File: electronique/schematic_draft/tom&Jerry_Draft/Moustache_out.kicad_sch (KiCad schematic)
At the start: 4 parts, among them J2001 Conn_01x02

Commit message: Adding footprint V0.1
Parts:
- C2001: footprint (none) -> Capacitor_SMD:C_0402_1005Metric
- J2001: footprint (none) -> Connector_JST:JST_XH_S2B-XH-A-1_1x02_P2.50mm_Horizontal
- R2001, R2002: footprint (none) -> Resistor_SMD:R_0402_1005Metric
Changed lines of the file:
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@@
 			)
 		)
-		(property "Footprint" ""
+		(property "Footprint" "Resistor_SMD:R_0402_1005Metric"
 			(at 143.51 72.39 0)
 			(effects
@@
 			)
 		)
-		(property "Footprint" ""
+		(property "Footprint" "Connector_JST:JST_XH_S2B-XH-A-1_1x02_P2.50mm_Horizontal"
 			(at 156.21 77.47 0)
 			(effects
@@
 			)
 		)
-		(property "Footprint" ""
+		(property "Footprint" "Resistor_SMD:R_0402_1005Metric"
 			(at 151.13 67.31 0)
 			(effects
@@
 			)
 		)
-		(property "Footprint" ""
+		(property "Footprint" "Capacitor_SMD:C_0402_1005Metric"
 			(at 137.16 77.47 0)
 			(effects

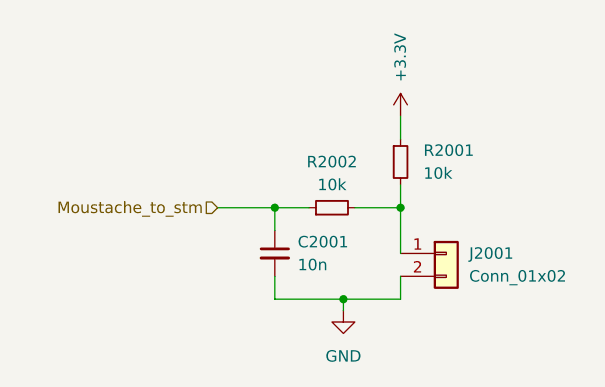
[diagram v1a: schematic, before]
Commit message: Ajout V2 TOF + MultiPCB Panalize
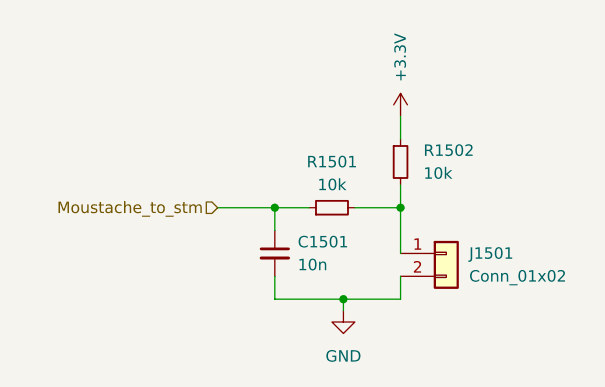
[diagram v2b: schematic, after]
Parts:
- renumbered C2001 to C1501, J2001 to J1501, R2002 to R1501, R2001 to R1502
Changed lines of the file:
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@@
 		(dnp no)
 		(fields_autoplaced yes)
-		(property "Reference" "R2002"
+		(property "Reference" "R1501"
 			(at 143.51 67.31 90)
 			(effects
@@
 			(project "tom&Jerry_Draft"
 				(path "/d6e3fbeb-d028-494d-83bf-2e4a8b12578d/ac7f7f04-c418-4551-b204-a999b9c3c440/4a942aeb-0f5a-4b74-98aa-4f22cccd5125"
-					(reference "R2002")
-					(unit 1)
-				)
-				(path "/d6e3fbeb-d028-494d-83bf-2e4a8b12578d/ac7f7f04-c418-4551-b204-a999b9c3c440/a23499ad-e269-4d60-8a7e-fdf0e52e9311"
-					(reference "R1702")
-					(unit 1)
-				)
-				(path "/d6e3fbeb-d028-494d-83bf-2e4a8b12578d/ac7f7f04-c418-4551-b204-a999b9c3c440/e8ed5780-2114-4427-a772-5bf6fa774e5b"
-					(reference "R1902")
-					(unit 1)
-				)
-				(path "/d6e3fbeb-d028-494d-83bf-2e4a8b12578d/ac7f7f04-c418-4551-b204-a999b9c3c440/e9c92678-eab0-4500-8304-4b18da6b06b1"
-					(reference "R1802")
+					(reference "R1501")
+					(unit 1)
+				)
+				(path "/d6e3fbeb-d028-494d-83bf-2e4a8b12578d/ac7f7f04-c418-4551-b204-a999b9c3c440/a23499ad-e269-4d60-8a7e-fdf0e52e9311"
+					(reference "R1201")
+					(unit 1)
+				)
+				(path "/d6e3fbeb-d028-494d-83bf-2e4a8b12578d/ac7f7f04-c418-4551-b204-a999b9c3c440/e8ed5780-2114-4427-a772-5bf6fa774e5b"
+					(reference "R1401")
+					(unit 1)
+				)
+				(path "/d6e3fbeb-d028-494d-83bf-2e4a8b12578d/ac7f7f04-c418-4551-b204-a999b9c3c440/e9c92678-eab0-4500-8304-4b18da6b06b1"
+					(reference "R1301")
 					(unit 1)
 				)
@@
 		(dnp no)
 		(fields_autoplaced yes)
-		(property "Reference" "J2001"
+		(property "Reference" "J1501"
 			(at 158.75 77.4699 0)
 			(effects
@@
 			(project "tom&Jerry_Draft"
 				(path "/d6e3fbeb-d028-494d-83bf-2e4a8b12578d/ac7f7f04-c418-4551-b204-a999b9c3c440/4a942aeb-0f5a-4b74-98aa-4f22cccd5125"
-					(reference "J2001")
-					(unit 1)
-				)
-				(path "/d6e3fbeb-d028-494d-83bf-2e4a8b12578d/ac7f7f04-c418-4551-b204-a999b9c3c440/a23499ad-e269-4d60-8a7e-fdf0e52e9311"
-					(reference "J1701")
-					(unit 1)
-				)
-				(path "/d6e3fbeb-d028-494d-83bf-2e4a8b12578d/ac7f7f04-c418-4551-b204-a999b9c3c440/e8ed5780-2114-4427-a772-5bf6fa774e5b"
-					(reference "J1901")
-					(unit 1)
-				)
-				(path "/d6e3fbeb-d028-494d-83bf-2e4a8b12578d/ac7f7f04-c418-4551-b204-a999b9c3c440/e9c92678-eab0-4500-8304-4b18da6b06b1"
-					(reference "J1801")
+					(reference "J1501")
+					(unit 1)
+				)
+				(path "/d6e3fbeb-d028-494d-83bf-2e4a8b12578d/ac7f7f04-c418-4551-b204-a999b9c3c440/a23499ad-e269-4d60-8a7e-fdf0e52e9311"
+					(reference "J1201")
+					(unit 1)
+				)
+				(path "/d6e3fbeb-d028-494d-83bf-2e4a8b12578d/ac7f7f04-c418-4551-b204-a999b9c3c440/e8ed5780-2114-4427-a772-5bf6fa774e5b"
+					(reference "J1401")
+					(unit 1)
+				)
+				(path "/d6e3fbeb-d028-494d-83bf-2e4a8b12578d/ac7f7f04-c418-4551-b204-a999b9c3c440/e9c92678-eab0-4500-8304-4b18da6b06b1"
+					(reference "J1301")
 					(unit 1)
 				)
@@
 		(dnp no)
 		(fields_autoplaced yes)
-		(property "Reference" "R2001"
+		(property "Reference" "R1502"
 			(at 153.67 66.0399 0)
 			(effects
@@
 			(project "tom&Jerry_Draft"
 				(path "/d6e3fbeb-d028-494d-83bf-2e4a8b12578d/ac7f7f04-c418-4551-b204-a999b9c3c440/4a942aeb-0f5a-4b74-98aa-4f22cccd5125"
-					(reference "R2001")
-					(unit 1)
-				)
-				(path "/d6e3fbeb-d028-494d-83bf-2e4a8b12578d/ac7f7f04-c418-4551-b204-a999b9c3c440/a23499ad-e269-4d60-8a7e-fdf0e52e9311"
-					(reference "R1701")
-					(unit 1)
-				)
-				(path "/d6e3fbeb-d028-494d-83bf-2e4a8b12578d/ac7f7f04-c418-4551-b204-a999b9c3c440/e8ed5780-2114-4427-a772-5bf6fa774e5b"
-					(reference "R1901")
-					(unit 1)
-				)
-				(path "/d6e3fbeb-d028-494d-83bf-2e4a8b12578d/ac7f7f04-c418-4551-b204-a999b9c3c440/e9c92678-eab0-4500-8304-4b18da6b06b1"
-					(reference "R1801")
+					(reference "R1502")
+					(unit 1)
+				)
+				(path "/d6e3fbeb-d028-494d-83bf-2e4a8b12578d/ac7f7f04-c418-4551-b204-a999b9c3c440/a23499ad-e269-4d60-8a7e-fdf0e52e9311"
+					(reference "R1202")
+					(unit 1)
+				)
+				(path "/d6e3fbeb-d028-494d-83bf-2e4a8b12578d/ac7f7f04-c418-4551-b204-a999b9c3c440/e8ed5780-2114-4427-a772-5bf6fa774e5b"
+					(reference "R1402")
+					(unit 1)
+				)
+				(path "/d6e3fbeb-d028-494d-83bf-2e4a8b12578d/ac7f7f04-c418-4551-b204-a999b9c3c440/e9c92678-eab0-4500-8304-4b18da6b06b1"
+					(reference "R1302")
 					(unit 1)
 				)
@@
 		(dnp no)
 		(fields_autoplaced yes)
-		(property "Reference" "#PWR02002"
+		(property "Reference" "#PWR01501"
 			(at 144.78 90.17 0)
 			(effects
@@
 			(project "tom&Jerry_Draft"
 				(path "/d6e3fbeb-d028-494d-83bf-2e4a8b12578d/ac7f7f04-c418-4551-b204-a999b9c3c440/4a942aeb-0f5a-4b74-98aa-4f22cccd5125"
-					(reference "#PWR02002")
-					(unit 1)
-				)
-				(path "/d6e3fbeb-d028-494d-83bf-2e4a8b12578d/ac7f7f04-c418-4551-b204-a999b9c3c440/a23499ad-e269-4d60-8a7e-fdf0e52e9311"
-					(reference "#PWR01702")
-					(unit 1)
-				)
-				(path "/d6e3fbeb-d028-494d-83bf-2e4a8b12578d/ac7f7f04-c418-4551-b204-a999b9c3c440/e8ed5780-2114-4427-a772-5bf6fa774e5b"
-					(reference "#PWR01902")
-					(unit 1)
-				)
-				(path "/d6e3fbeb-d028-494d-83bf-2e4a8b12578d/ac7f7f04-c418-4551-b204-a999b9c3c440/e9c92678-eab0-4500-8304-4b18da6b06b1"
-					(reference "#PWR01802")
+					(reference "#PWR01501")
+					(unit 1)
+				)
+				(path "/d6e3fbeb-d028-494d-83bf-2e4a8b12578d/ac7f7f04-c418-4551-b204-a999b9c3c440/a23499ad-e269-4d60-8a7e-fdf0e52e9311"
+					(reference "#PWR01201")
+					(unit 1)
+				)
+				(path "/d6e3fbeb-d028-494d-83bf-2e4a8b12578d/ac7f7f04-c418-4551-b204-a999b9c3c440/e8ed5780-2114-4427-a772-5bf6fa774e5b"
+					(reference "#PWR01401")
+					(unit 1)
+				)
+				(path "/d6e3fbeb-d028-494d-83bf-2e4a8b12578d/ac7f7f04-c418-4551-b204-a999b9c3c440/e9c92678-eab0-4500-8304-4b18da6b06b1"
+					(reference "#PWR01301")
 					(unit 1)
 				)
@@
 		(dnp no)
 		(fields_autoplaced yes)
-		(property "Reference" "C2001"
+		(property "Reference" "C1501"
 			(at 139.7 76.2062 0)
 			(effects
@@
 			(project "tom&Jerry_Draft"
 				(path "/d6e3fbeb-d028-494d-83bf-2e4a8b12578d/ac7f7f04-c418-4551-b204-a999b9c3c440/4a942aeb-0f5a-4b74-98aa-4f22cccd5125"
-					(reference "C2001")
-					(unit 1)
-				)
-				(path "/d6e3fbeb-d028-494d-83bf-2e4a8b12578d/ac7f7f04-c418-4551-b204-a999b9c3c440/a23499ad-e269-4d60-8a7e-fdf0e52e9311"
-					(reference "C1701")
-					(unit 1)
-				)
-				(path "/d6e3fbeb-d028-494d-83bf-2e4a8b12578d/ac7f7f04-c418-4551-b204-a999b9c3c440/e8ed5780-2114-4427-a772-5bf6fa774e5b"
-					(reference "C1901")
-					(unit 1)
-				)
-				(path "/d6e3fbeb-d028-494d-83bf-2e4a8b12578d/ac7f7f04-c418-4551-b204-a999b9c3c440/e9c92678-eab0-4500-8304-4b18da6b06b1"
-					(reference "C1801")
+					(reference "C1501")
+					(unit 1)
+				)
+				(path "/d6e3fbeb-d028-494d-83bf-2e4a8b12578d/ac7f7f04-c418-4551-b204-a999b9c3c440/a23499ad-e269-4d60-8a7e-fdf0e52e9311"
+					(reference "C1201")
+					(unit 1)
+				)
+				(path "/d6e3fbeb-d028-494d-83bf-2e4a8b12578d/ac7f7f04-c418-4551-b204-a999b9c3c440/e8ed5780-2114-4427-a772-5bf6fa774e5b"
+					(reference "C1401")
+					(unit 1)
+				)
+				(path "/d6e3fbeb-d028-494d-83bf-2e4a8b12578d/ac7f7f04-c418-4551-b204-a999b9c3c440/e9c92678-eab0-4500-8304-4b18da6b06b1"
+					(reference "C1301")
 					(unit 1)
 				)
@@
 		(on_board yes)
 		(dnp no)
-		(property "Reference" "#PWR02001"
+		(property "Reference" "#PWR01502"
 			(at 151.13 66.04 0)
 			(effects
@@
 			(project "tom&Jerry_Draft"
 				(path "/d6e3fbeb-d028-494d-83bf-2e4a8b12578d/ac7f7f04-c418-4551-b204-a999b9c3c440/4a942aeb-0f5a-4b74-98aa-4f22cccd5125"
-					(reference "#PWR02001")
-					(unit 1)
-				)
-				(path "/d6e3fbeb-d028-494d-83bf-2e4a8b12578d/ac7f7f04-c418-4551-b204-a999b9c3c440/a23499ad-e269-4d60-8a7e-fdf0e52e9311"
-					(reference "#PWR01701")
-					(unit 1)
-				)
-				(path "/d6e3fbeb-d028-494d-83bf-2e4a8b12578d/ac7f7f04-c418-4551-b204-a999b9c3c440/e8ed5780-2114-4427-a772-5bf6fa774e5b"
-					(reference "#PWR01901")
-					(unit 1)
-				)
-				(path "/d6e3fbeb-d028-494d-83bf-2e4a8b12578d/ac7f7f04-c418-4551-b204-a999b9c3c440/e9c92678-eab0-4500-8304-4b18da6b06b1"
-					(reference "#PWR01801")
-					(unit 1)
-				)
+					(reference "#PWR01502")
+					(unit 1)
+				)
+				(path "/d6e3fbeb-d028-494d-83bf-2e4a8b12578d/ac7f7f04-c418-4551-b204-a999b9c3c440/a23499ad-e269-4d60-8a7e-fdf0e52e9311"
+					(reference "#PWR01202")
+					(unit 1)
+				)
+				(path "/d6e3fbeb-d028-494d-83bf-2e4a8b12578d/ac7f7f04-c418-4551-b204-a999b9c3c440/e8ed5780-2114-4427-a772-5bf6fa774e5b"
+					(reference "#PWR01402")
+					(unit 1)
+				)
+				(path "/d6e3fbeb-d028-494d-83bf-2e4a8b12578d/ac7f7f04-c418-4551-b204-a999b9c3c440/e9c92678-eab0-4500-8304-4b18da6b06b1"
+					(reference "#PWR01302")
+					(unit 1)
+				)

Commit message: Routage Signal Complet - PCB V2.0
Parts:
- renumbered C1501 to C1601, J1501 to J1601, R1502 to R1601, R1501 to R1602
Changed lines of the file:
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@@
 		(dnp no)
 		(fields_autoplaced yes)
-		(property "Reference" "R1501"
+		(property "Reference" "R1602"
 			(at 143.51 67.31 90)
 			(effects
@@
 			(project "tom&Jerry_Draft"
 				(path "/d6e3fbeb-d028-494d-83bf-2e4a8b12578d/ac7f7f04-c418-4551-b204-a999b9c3c440/4a942aeb-0f5a-4b74-98aa-4f22cccd5125"
-					(reference "R1501")
-					(unit 1)
-				)
-				(path "/d6e3fbeb-d028-494d-83bf-2e4a8b12578d/ac7f7f04-c418-4551-b204-a999b9c3c440/a23499ad-e269-4d60-8a7e-fdf0e52e9311"
-					(reference "R1201")
-					(unit 1)
-				)
-				(path "/d6e3fbeb-d028-494d-83bf-2e4a8b12578d/ac7f7f04-c418-4551-b204-a999b9c3c440/e8ed5780-2114-4427-a772-5bf6fa774e5b"
-					(reference "R1401")
-					(unit 1)
-				)
-				(path "/d6e3fbeb-d028-494d-83bf-2e4a8b12578d/ac7f7f04-c418-4551-b204-a999b9c3c440/e9c92678-eab0-4500-8304-4b18da6b06b1"
-					(reference "R1301")
+					(reference "R1602")
+					(unit 1)
+				)
+				(path "/d6e3fbeb-d028-494d-83bf-2e4a8b12578d/ac7f7f04-c418-4551-b204-a999b9c3c440/a23499ad-e269-4d60-8a7e-fdf0e52e9311"
+					(reference "R1302")
+					(unit 1)
+				)
+				(path "/d6e3fbeb-d028-494d-83bf-2e4a8b12578d/ac7f7f04-c418-4551-b204-a999b9c3c440/e8ed5780-2114-4427-a772-5bf6fa774e5b"
+					(reference "R1502")
+					(unit 1)
+				)
+				(path "/d6e3fbeb-d028-494d-83bf-2e4a8b12578d/ac7f7f04-c418-4551-b204-a999b9c3c440/e9c92678-eab0-4500-8304-4b18da6b06b1"
+					(reference "R1402")
 					(unit 1)
 				)
@@
 		(dnp no)
 		(fields_autoplaced yes)
-		(property "Reference" "J1501"
+		(property "Reference" "J1601"
 			(at 158.75 77.4699 0)
 			(effects
@@
 			(project "tom&Jerry_Draft"
 				(path "/d6e3fbeb-d028-494d-83bf-2e4a8b12578d/ac7f7f04-c418-4551-b204-a999b9c3c440/4a942aeb-0f5a-4b74-98aa-4f22cccd5125"
+					(reference "J1601")
+					(unit 1)
+				)
+				(path "/d6e3fbeb-d028-494d-83bf-2e4a8b12578d/ac7f7f04-c418-4551-b204-a999b9c3c440/a23499ad-e269-4d60-8a7e-fdf0e52e9311"
+					(reference "J1301")
+					(unit 1)
+				)
+				(path "/d6e3fbeb-d028-494d-83bf-2e4a8b12578d/ac7f7f04-c418-4551-b204-a999b9c3c440/e8ed5780-2114-4427-a772-5bf6fa774e5b"
 					(reference "J1501")
 					(unit 1)
 				)
-				(path "/d6e3fbeb-d028-494d-83bf-2e4a8b12578d/ac7f7f04-c418-4551-b204-a999b9c3c440/a23499ad-e269-4d60-8a7e-fdf0e52e9311"
-					(reference "J1201")
-					(unit 1)
-				)
-				(path "/d6e3fbeb-d028-494d-83bf-2e4a8b12578d/ac7f7f04-c418-4551-b204-a999b9c3c440/e8ed5780-2114-4427-a772-5bf6fa774e5b"
+				(path "/d6e3fbeb-d028-494d-83bf-2e4a8b12578d/ac7f7f04-c418-4551-b204-a999b9c3c440/e9c92678-eab0-4500-8304-4b18da6b06b1"
 					(reference "J1401")
-					(unit 1)
-				)
-				(path "/d6e3fbeb-d028-494d-83bf-2e4a8b12578d/ac7f7f04-c418-4551-b204-a999b9c3c440/e9c92678-eab0-4500-8304-4b18da6b06b1"
-					(reference "J1301")
 					(unit 1)
 				)
@@
 		(dnp no)
 		(fields_autoplaced yes)
-		(property "Reference" "R1502"
+		(property "Reference" "R1601"
 			(at 153.67 66.0399 0)
 			(effects
@@
 			(project "tom&Jerry_Draft"
 				(path "/d6e3fbeb-d028-494d-83bf-2e4a8b12578d/ac7f7f04-c418-4551-b204-a999b9c3c440/4a942aeb-0f5a-4b74-98aa-4f22cccd5125"
-					(reference "R1502")
-					(unit 1)
-				)
-				(path "/d6e3fbeb-d028-494d-83bf-2e4a8b12578d/ac7f7f04-c418-4551-b204-a999b9c3c440/a23499ad-e269-4d60-8a7e-fdf0e52e9311"
-					(reference "R1202")
-					(unit 1)
-				)
-				(path "/d6e3fbeb-d028-494d-83bf-2e4a8b12578d/ac7f7f04-c418-4551-b204-a999b9c3c440/e8ed5780-2114-4427-a772-5bf6fa774e5b"
-					(reference "R1402")
-					(unit 1)
-				)
-				(path "/d6e3fbeb-d028-494d-83bf-2e4a8b12578d/ac7f7f04-c418-4551-b204-a999b9c3c440/e9c92678-eab0-4500-8304-4b18da6b06b1"
-					(reference "R1302")
+					(reference "R1601")
+					(unit 1)
+				)
+				(path "/d6e3fbeb-d028-494d-83bf-2e4a8b12578d/ac7f7f04-c418-4551-b204-a999b9c3c440/a23499ad-e269-4d60-8a7e-fdf0e52e9311"
+					(reference "R1301")
+					(unit 1)
+				)
+				(path "/d6e3fbeb-d028-494d-83bf-2e4a8b12578d/ac7f7f04-c418-4551-b204-a999b9c3c440/e8ed5780-2114-4427-a772-5bf6fa774e5b"
+					(reference "R1501")
+					(unit 1)
+				)
+				(path "/d6e3fbeb-d028-494d-83bf-2e4a8b12578d/ac7f7f04-c418-4551-b204-a999b9c3c440/e9c92678-eab0-4500-8304-4b18da6b06b1"
+					(reference "R1401")
 					(unit 1)
 				)
@@
 		(dnp no)
 		(fields_autoplaced yes)
-		(property "Reference" "#PWR01501"
+		(property "Reference" "#PWR01602"
 			(at 144.78 90.17 0)
 			(effects
@@
 			(project "tom&Jerry_Draft"
 				(path "/d6e3fbeb-d028-494d-83bf-2e4a8b12578d/ac7f7f04-c418-4551-b204-a999b9c3c440/4a942aeb-0f5a-4b74-98aa-4f22cccd5125"
-					(reference "#PWR01501")
-					(unit 1)
-				)
-				(path "/d6e3fbeb-d028-494d-83bf-2e4a8b12578d/ac7f7f04-c418-4551-b204-a999b9c3c440/a23499ad-e269-4d60-8a7e-fdf0e52e9311"
-					(reference "#PWR01201")
-					(unit 1)
-				)
-				(path "/d6e3fbeb-d028-494d-83bf-2e4a8b12578d/ac7f7f04-c418-4551-b204-a999b9c3c440/e8ed5780-2114-4427-a772-5bf6fa774e5b"
-					(reference "#PWR01401")
-					(unit 1)
-				)
-				(path "/d6e3fbeb-d028-494d-83bf-2e4a8b12578d/ac7f7f04-c418-4551-b204-a999b9c3c440/e9c92678-eab0-4500-8304-4b18da6b06b1"
-					(reference "#PWR01301")
+					(reference "#PWR01602")
+					(unit 1)
+				)
+				(path "/d6e3fbeb-d028-494d-83bf-2e4a8b12578d/ac7f7f04-c418-4551-b204-a999b9c3c440/a23499ad-e269-4d60-8a7e-fdf0e52e9311"
+					(reference "#PWR01302")
+					(unit 1)
+				)
+				(path "/d6e3fbeb-d028-494d-83bf-2e4a8b12578d/ac7f7f04-c418-4551-b204-a999b9c3c440/e8ed5780-2114-4427-a772-5bf6fa774e5b"
+					(reference "#PWR01502")
+					(unit 1)
+				)
+				(path "/d6e3fbeb-d028-494d-83bf-2e4a8b12578d/ac7f7f04-c418-4551-b204-a999b9c3c440/e9c92678-eab0-4500-8304-4b18da6b06b1"
+					(reference "#PWR01402")
 					(unit 1)
 				)
@@
 		(dnp no)
 		(fields_autoplaced yes)
-		(property "Reference" "C1501"
+		(property "Reference" "C1601"
 			(at 139.7 76.2062 0)
 			(effects
@@
 			(project "tom&Jerry_Draft"
 				(path "/d6e3fbeb-d028-494d-83bf-2e4a8b12578d/ac7f7f04-c418-4551-b204-a999b9c3c440/4a942aeb-0f5a-4b74-98aa-4f22cccd5125"
+					(reference "C1601")
+					(unit 1)
+				)
+				(path "/d6e3fbeb-d028-494d-83bf-2e4a8b12578d/ac7f7f04-c418-4551-b204-a999b9c3c440/a23499ad-e269-4d60-8a7e-fdf0e52e9311"
+					(reference "C1301")
+					(unit 1)
+				)
+				(path "/d6e3fbeb-d028-494d-83bf-2e4a8b12578d/ac7f7f04-c418-4551-b204-a999b9c3c440/e8ed5780-2114-4427-a772-5bf6fa774e5b"
 					(reference "C1501")
 					(unit 1)
 				)
-				(path "/d6e3fbeb-d028-494d-83bf-2e4a8b12578d/ac7f7f04-c418-4551-b204-a999b9c3c440/a23499ad-e269-4d60-8a7e-fdf0e52e9311"
-					(reference "C1201")
-					(unit 1)
-				)
-				(path "/d6e3fbeb-d028-494d-83bf-2e4a8b12578d/ac7f7f04-c418-4551-b204-a999b9c3c440/e8ed5780-2114-4427-a772-5bf6fa774e5b"
+				(path "/d6e3fbeb-d028-494d-83bf-2e4a8b12578d/ac7f7f04-c418-4551-b204-a999b9c3c440/e9c92678-eab0-4500-8304-4b18da6b06b1"
 					(reference "C1401")
-					(unit 1)
-				)
-				(path "/d6e3fbeb-d028-494d-83bf-2e4a8b12578d/ac7f7f04-c418-4551-b204-a999b9c3c440/e9c92678-eab0-4500-8304-4b18da6b06b1"
-					(reference "C1301")
 					(unit 1)
 				)
@@
 		(on_board yes)
 		(dnp no)
-		(property "Reference" "#PWR01502"
+		(property "Reference" "#PWR01601"
 			(at 151.13 66.04 0)
 			(effects
@@
 			(project "tom&Jerry_Draft"
 				(path "/d6e3fbeb-d028-494d-83bf-2e4a8b12578d/ac7f7f04-c418-4551-b204-a999b9c3c440/4a942aeb-0f5a-4b74-98aa-4f22cccd5125"
-					(reference "#PWR01502")
-					(unit 1)
-				)
-				(path "/d6e3fbeb-d028-494d-83bf-2e4a8b12578d/ac7f7f04-c418-4551-b204-a999b9c3c440/a23499ad-e269-4d60-8a7e-fdf0e52e9311"
-					(reference "#PWR01202")
-					(unit 1)
-				)
-				(path "/d6e3fbeb-d028-494d-83bf-2e4a8b12578d/ac7f7f04-c418-4551-b204-a999b9c3c440/e8ed5780-2114-4427-a772-5bf6fa774e5b"
-					(reference "#PWR01402")
-					(unit 1)
-				)
-				(path "/d6e3fbeb-d028-494d-83bf-2e4a8b12578d/ac7f7f04-c418-4551-b204-a999b9c3c440/e9c92678-eab0-4500-8304-4b18da6b06b1"
-					(reference "#PWR01302")
-					(unit 1)
-				)
+					(reference "#PWR01601")
+					(unit 1)
+				)
+				(path "/d6e3fbeb-d028-494d-83bf-2e4a8b12578d/ac7f7f04-c418-4551-b204-a999b9c3c440/a23499ad-e269-4d60-8a7e-fdf0e52e9311"
+					(reference "#PWR01301")
+					(unit 1)
+				)
+				(path "/d6e3fbeb-d028-494d-83bf-2e4a8b12578d/ac7f7f04-c418-4551-b204-a999b9c3c440/e8ed5780-2114-4427-a772-5bf6fa774e5b"
+					(reference "#PWR01501")
+					(unit 1)
+				)
+				(path "/d6e3fbeb-d028-494d-83bf-2e4a8b12578d/ac7f7f04-c418-4551-b204-a999b9c3c440/e9c92678-eab0-4500-8304-4b18da6b06b1"
+					(reference "#PWR01401")
+					(unit 1)
+				)
